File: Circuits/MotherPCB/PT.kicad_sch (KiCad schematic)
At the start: 1 part, among them J2 Raspberry_Pi_2_3

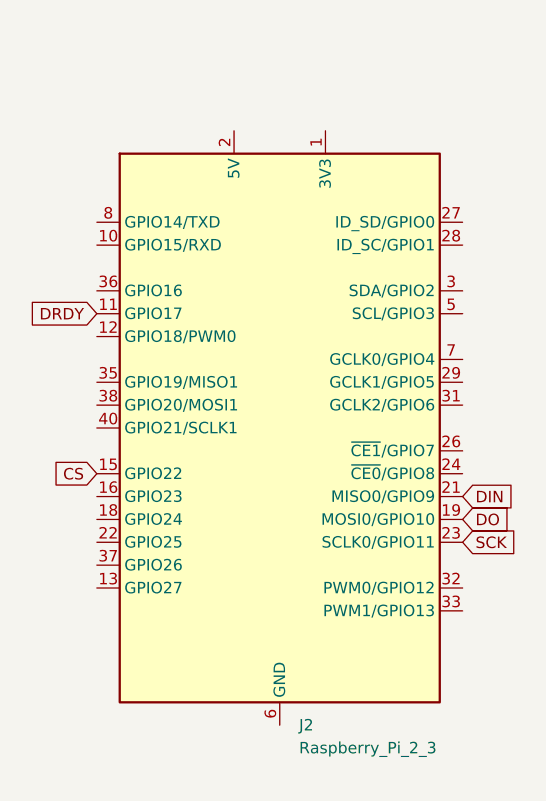
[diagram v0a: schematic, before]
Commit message: Added footprint for ATTiny85 module, added schematic for oil injector circuit
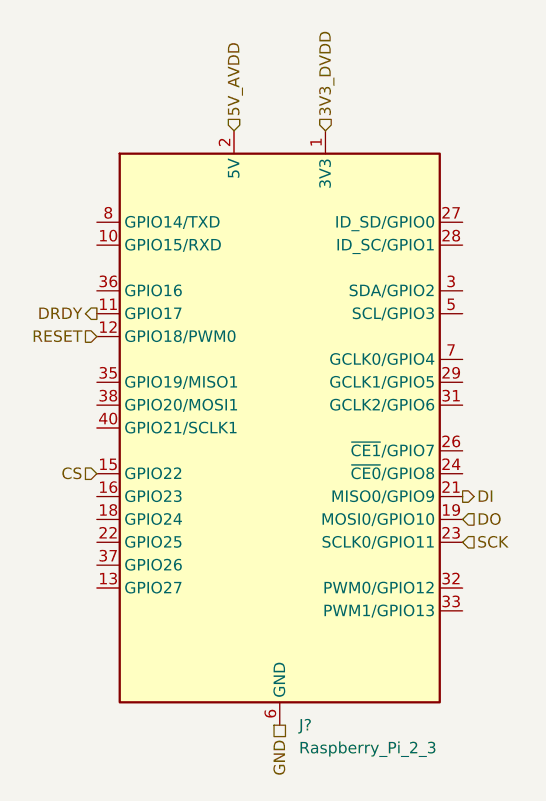
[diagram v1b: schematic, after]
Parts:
- renumbered J2 to J?
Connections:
- net 3V3_DVDD: now reaches J?.1 (3V3), J?.17 (3V3)
- net RESET: now reaches J?.12 (GPIO18/PWM0)
- net GND: now reaches J?.14 (GND), J?.20 (GND), J?.25 (GND), J?.30 (GND), J?.34 (GND), J?.39 (GND), J?.6 (GND), J?.9 (GND)
- net 5V_AVDD: now reaches J?.2 (5V), J?.4 (5V)
- net DIN renamed DI
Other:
- company: (none) -> Project Arka
- title: (none) -> Pressure Transducer Hat Interface
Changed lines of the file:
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@@
 	(generator_version "9.0")
 	(paper "A4")
-	(global_label "DRDY"
-		(shape input)
+	(title_block
+		(title "Pressure Transducer Hat Interface")
+		(date "2026-01-26")
+		(rev "1.0")
+		(company "Project Arka")
+	)
+	(hierarchical_label "5V_AVDD"
+		(shape input)
+		(at 133.35 68.58 90)
+		(effects
+			(font
+				(size 1.27 1.27)
+			)
+			(justify left)
+		)
+	)
+	(hierarchical_label "SCK"
+		(shape input)
+		(at 158.75 114.3 0)
+		(effects
+			(font
+				(size 1.27 1.27)
+			)
+			(justify left)
+		)
+	)
+	(hierarchical_label "DI"
+		(shape output)
+		(at 158.75 109.22 0)
+		(effects
+			(font
+				(size 1.27 1.27)
+			)
+			(justify left)
+		)
+	)
+	(hierarchical_label "DRDY"
+		(shape output)
 		(at 118.11 88.9 180)
-		(fields_autoplaced yes)
-		(effects
-			(font
-				(size 1.27 1.27)
-			)
-			(justify right)
-		)
-		(property "Intersheetrefs" "${INTERSHEET_REFS}"
-			(at 110.2262 88.9 0)
-			(effects
-				(font
-					(size 1.27 1.27)
-				)
-				(justify right)
-				(hide yes)
-			)
-		)
-	)
-	(global_label "CS"
+		(effects
+			(font
+				(size 1.27 1.27)
+			)
+			(justify right)
+		)
+	)
+	(hierarchical_label "DO"
+		(shape input)
+		(at 158.75 111.76 0)
+		(effects
+			(font
+				(size 1.27 1.27)
+			)
+			(justify left)
+		)
+	)
+	(hierarchical_label "GND"
+		(shape passive)
+		(at 138.43 134.62 270)
+		(effects
+			(font
+				(size 1.27 1.27)
+			)
+			(justify right)
+		)
+	)
+	(hierarchical_label "RESET"
+		(shape input)
+		(at 118.11 91.44 180)
+		(effects
+			(font
+				(size 1.27 1.27)
+			)
+			(justify right)
+		)
+	)
+	(hierarchical_label "CS"
 		(shape input)
 		(at 118.11 106.68 180)
-		(fields_autoplaced yes)
-		(effects
-			(font
-				(size 1.27 1.27)
-			)
-			(justify right)
-		)
-		(property "Intersheetrefs" "${INTERSHEET_REFS}"
-			(at 112.6453 106.68 0)
-			(effects
-				(font
-					(size 1.27 1.27)
-				)
-				(justify right)
-				(hide yes)
-			)
-		)
-	)
-	(global_label "DIN"
-		(shape input)
-		(at 158.75 109.22 0)
-		(fields_autoplaced yes)
-		(effects
-			(font
-				(size 1.27 1.27)
-			)
-			(justify left)
-		)
-		(property "Intersheetrefs" "${INTERSHEET_REFS}"
-			(at 164.9405 109.22 0)
-			(effects
-				(font
-					(size 1.27 1.27)
-				)
-				(justify left)
-				(hide yes)
-			)
-		)
-	)
-	(global_label "DO"
-		(shape input)
-		(at 158.75 111.76 0)
-		(fields_autoplaced yes)
-		(effects
-			(font
-				(size 1.27 1.27)
-			)
-			(justify left)
-		)
-		(property "Intersheetrefs" "${INTERSHEET_REFS}"
-			(at 164.3357 111.76 0)
-			(effects
-				(font
-					(size 1.27 1.27)
-				)
-				(justify left)
-				(hide yes)
-			)
-		)
-	)
-	(global_label "SCK"
-		(shape input)
-		(at 158.75 114.3 0)
-		(fields_autoplaced yes)
-		(effects
-			(font
-				(size 1.27 1.27)
-			)
-			(justify left)
-		)
-		(property "Intersheetrefs" "${INTERSHEET_REFS}"
-			(at 165.4847 114.3 0)
-			(effects
-				(font
-					(size 1.27 1.27)
-				)
-				(justify left)
-				(hide yes)
-			)
+		(effects
+			(font
+				(size 1.27 1.27)
+			)
+			(justify right)
+		)
+	)
+	(hierarchical_label "3V3_DVDD"
+		(shape input)
+		(at 143.51 68.58 90)
+		(effects
+			(font
+				(size 1.27 1.27)
+			)
+			(justify left)
 		)
 	)
@@
 		(dnp no)
 		(fields_autoplaced yes)
-		(property "Reference" "J2"
+		(property "Reference" "J?"
 			(at 140.5733 134.62 0)
 			(effects
@@
 		)
 		(instances
+			(project "PT"
+				(path "/7ba2d465-b15d-4d9e-ba6b-71034cc30fb1"
+					(reference "J?")
+					(unit 1)
+				)
+			)
 			(project ""
 				(path "/ab0f1194-a63d-4164-a2ac-f17f7396e885"
@@
 					(unit 1)
 				)
+			)
+			(project "MotherPCB"
+				(path "/ea485091-218e-4ddf-97d6-ebaac999a2f0/58b7763a-b863-498c-a2bf-e5a83db7c2fb"
+					(reference "J?")
+					(unit 1)
+				)

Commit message: Fixed some broken footprints
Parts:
- gave numbers to parts that had none: 1
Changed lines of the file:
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@@
 		(dnp no)
 		(fields_autoplaced yes)
-		(property "Reference" "J?"
+		(property "Reference" "J20"
 			(at 140.5733 134.62 0)
 			(effects
@@
 			(project "MotherPCB"
 				(path "/ea485091-218e-4ddf-97d6-ebaac999a2f0/58b7763a-b863-498c-a2bf-e5a83db7c2fb"
-					(reference "J?")
+					(reference "J20")
 					(unit 1)
 				)

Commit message: pcb completed with a clean DRC
first one it is let us pray it works
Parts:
- J20: footprint (none) -> Connector_PinHeader_2.54mm:PinHeader_2x20_P2.54mm_Vertical
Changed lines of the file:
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@@
 			)
 		)
-		(property "Footprint" ""
+		(property "Footprint" "Connector_PinHeader_2.54mm:PinHeader_2x20_P2.54mm_Vertical"
 			(at 138.43 101.6 0)
 			(effects

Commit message: PCB v2 um
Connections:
- no-connect marks 0 -> 26
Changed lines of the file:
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@@
 		(company "Project Arka")
+	)
+	(no_connect
+		(at 118.11 119.38)
+	)
+	(no_connect
+		(at 158.75 121.92)
+	)
+	(no_connect
+		(at 158.75 119.38)
+	)
+	(no_connect
+		(at 158.75 96.52)
+	)
+	(no_connect
+		(at 158.75 93.98)
+	)
+	(no_connect
+		(at 158.75 78.74)
+	)
+	(no_connect
+		(at 118.11 115.57)
+	)
+	(no_connect
+		(at 158.75 99.06)
+	)
+	(no_connect
+		(at 158.75 88.9)
+	)
+	(no_connect
+		(at 118.11 95.25)
+	)
+	(no_connect
+		(at 118.11 81.28)
+	)
+	(no_connect
+		(at 118.11 101.6)
+	)
+	(no_connect
+		(at 118.11 99.06)
+	)
+	(no_connect
+		(at 158.75 91.44)
+	)
+	(no_connect
+		(at 158.75 86.36)
+	)
+	(no_connect
+		(at 158.75 106.68)
+	)
+	(no_connect
+		(at 118.11 114.3)
+	)
+	(no_connect
+		(at 158.75 81.28)
+	)
+	(no_connect
+		(at 118.11 83.82)
+	)
+	(no_connect
+		(at 118.11 111.76)
+	)
+	(no_connect
+		(at 158.75 101.6)
+	)
+	(no_connect
+		(at 158.75 104.14)
+	)
+	(no_connect
+		(at 118.11 78.74)
+	)
+	(no_connect
+		(at 118.11 116.84)
+	)
+	(no_connect
+		(at 118.11 86.36)
+	)
+	(no_connect
+		(at 118.11 109.22)
 	)
 	(hierarchical_label "5V_AVDD"
